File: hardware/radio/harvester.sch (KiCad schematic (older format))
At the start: 39 parts, among them Q201 BSH105, U201 LTC3331

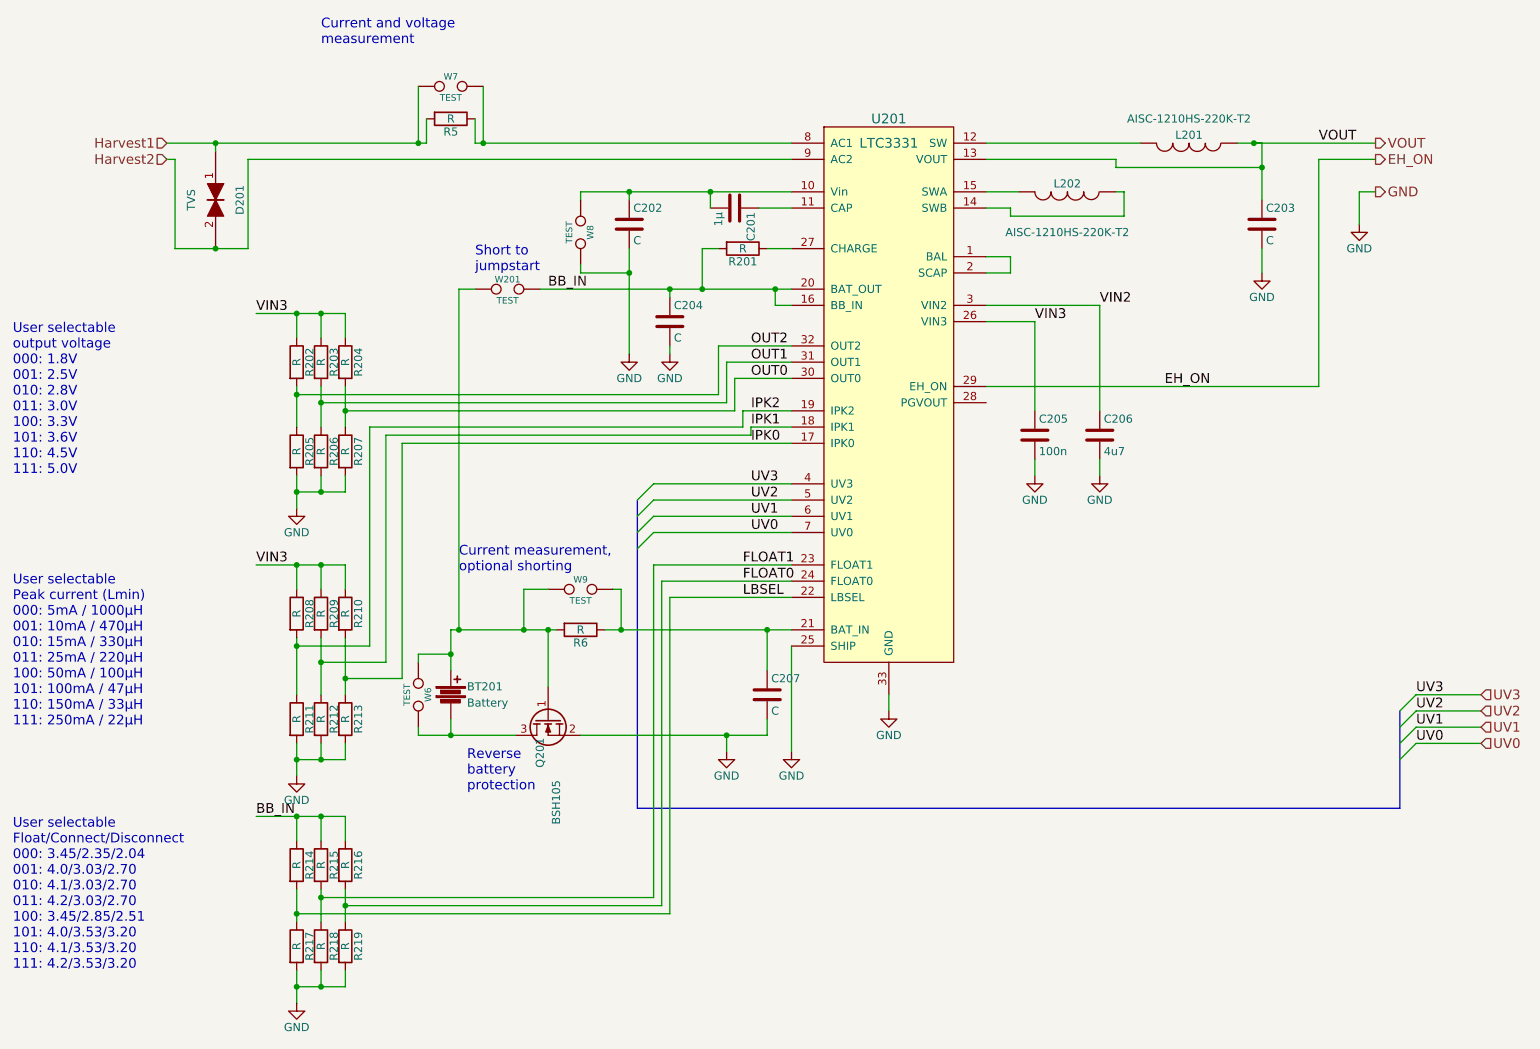
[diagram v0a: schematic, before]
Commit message: compress schematic for embedding images in thesis
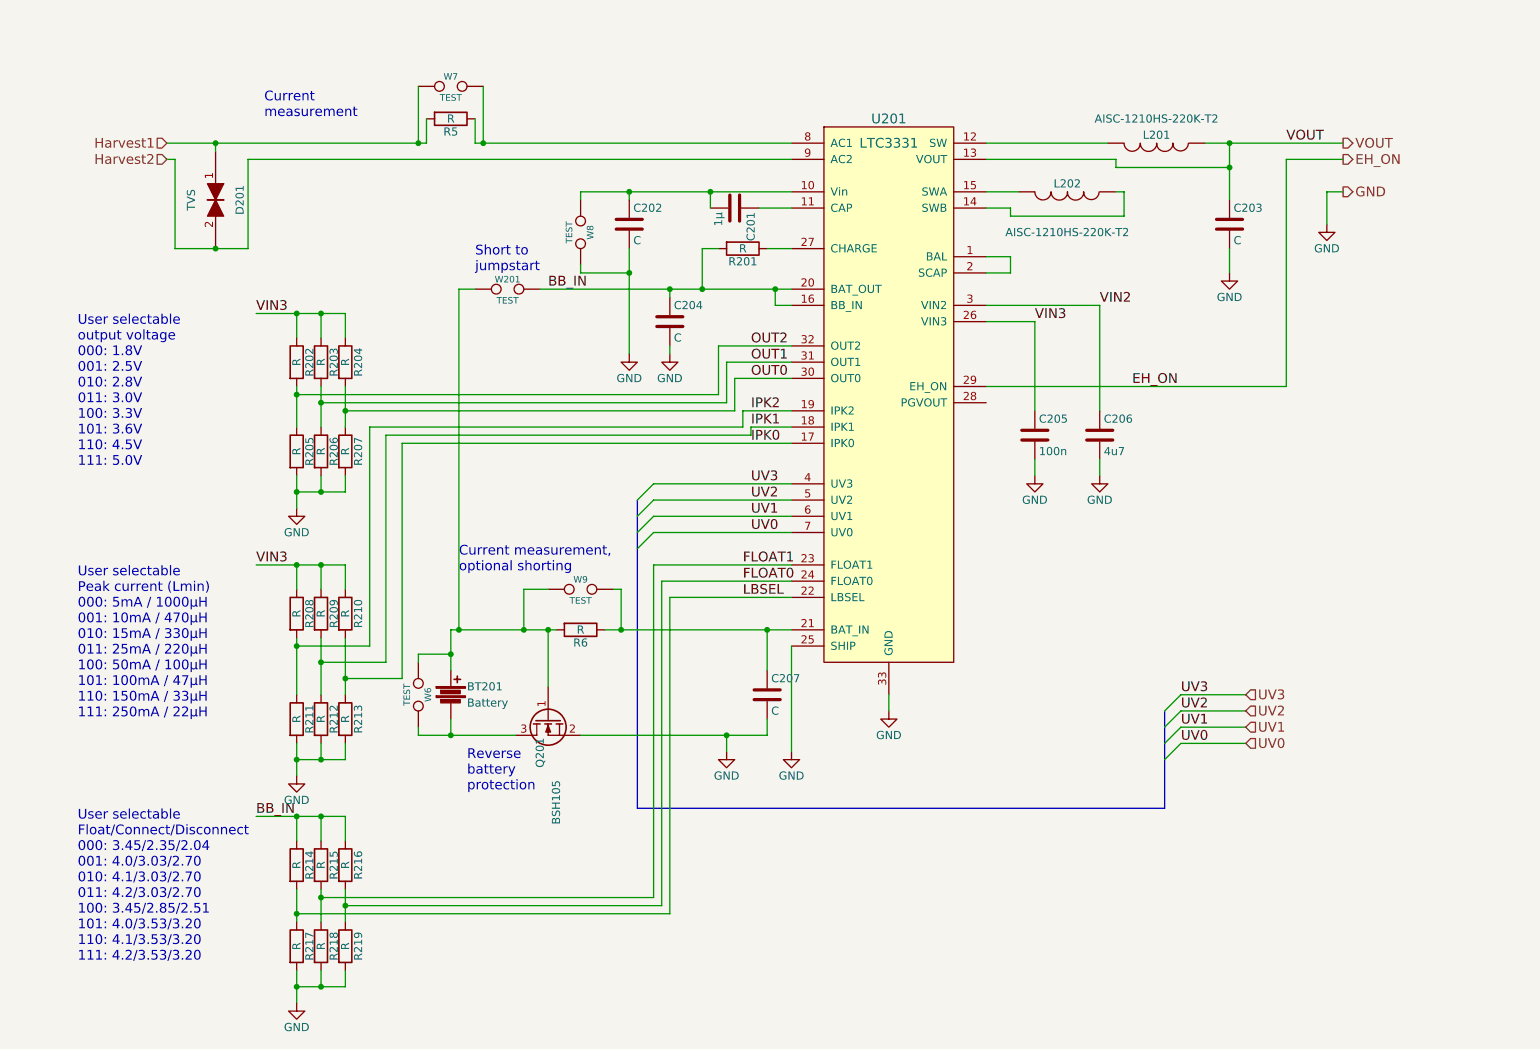
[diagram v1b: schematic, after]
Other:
- note added: "Current\nmeasurement"
- note removed: "Current and voltage \nmeasurement"
- moved on the sheet: C203, L201
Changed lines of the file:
@@
 	1    0    0    -1
 $EndComp
-Text Notes 1100 4250 0    60   ~ 0
+Text Notes 1500 4200 0    60   ~ 0
 User selectable \noutput voltage\n000: 1.8V\n001: 2.5V\n010: 2.8V\n011: 3.0V\n100: 3.3V\n101: 3.6V\n110: 4.5V\n111: 5.0V
 Text Label 2600 3250 0    60   ~ 0
@@
 	1    0    0    -1
 $EndComp
-Text Notes 1100 7300 0    60   ~ 0
+Text Notes 1500 7250 0    60   ~ 0
 User selectable \nFloat/Connect/Disconnect\n000: 3.45/2.35/2.04\n001: 4.0/3.03/2.70\n010: 4.1/3.03/2.70\n011: 4.2/3.03/2.70\n100: 3.45/2.85/2.51\n101: 4.0/3.53/3.20\n110: 4.1/3.53/3.20\n111: 4.2/3.53/3.20
 $Comp
@@
 	1    0    0    -1
 $EndComp
-Text Notes 1100 5800 0    60   ~ 0
+Text Notes 1500 5750 0    60   ~ 0
 User selectable \nPeak current (Lmin)\n000: 5mA / 1000µH\n001: 10mA / 470µH\n010: 15mA / 330µH\n011: 25mA / 220µH\n100: 50mA / 100µH\n101: 100mA / 47µH\n110: 150mA / 33µH\n111: 250mA / 22µH
 Text Label 5650 3450 0    60   ~ 0
@@
 L INDUCTOR L201
 U 1 1 55EA045E
-P 8350 2200
-F 0 "L201" V 8300 2200 50  0000 C CNN
-F 1 "AISC-1210HS-220K-T2" V 8200 2200 50  0000 C CNN
-F 2 "Resistors_SMD:R_1210" H 8350 2200 60  0001 C CNN
-F 3 "" H 8350 2200 60  0000 C CNN
-	1    8350 2200
+P 8150 2200
+F 0 "L201" V 8100 2200 50  0000 C CNN
+F 1 "AISC-1210HS-220K-T2" V 8000 2200 50  0000 C CNN
+F 2 "Resistors_SMD:R_1210" H 8150 2200 60  0001 C CNN
+F 3 "" H 8150 2200 60  0000 C CNN
+	1    8150 2200
 	0    1    1    0
 $EndComp
@@
 L C C203
 U 1 1 55EA08DD
-P 8800 2700
-F 0 "C203" H 8825 2800 50  0000 L CNN
-F 1 "C" H 8825 2600 50  0000 L CNN
-F 2 "Capacitors_SMD:C_0603" H 8838 2550 30  0001 C CNN
-F 3 "" H 8800 2700 60  0000 C CNN
-	1    8800 2700
+P 8600 2700
+F 0 "C203" H 8625 2800 50  0000 L CNN
+F 1 "C" H 8625 2600 50  0000 L CNN
+F 2 "Capacitors_SMD:C_0603" H 8638 2550 30  0001 C CNN
+F 3 "" H 8600 2700 60  0000 C CNN
+	1    8600 2700
 	1    0    0    -1
 $EndComp
@@
 L GND #PWR020
 U 1 1 55EA0A97
-P 8800 3000
-F 0 "#PWR020" H 8800 2750 50  0001 C CNN
-F 1 "GND" H 8800 2850 50  0000 C CNN
-F 2 "" H 8800 3000 60  0000 C CNN
-F 3 "" H 8800 3000 60  0000 C CNN
-	1    8800 3000
+P 8600 3000
+F 0 "#PWR020" H 8600 2750 50  0001 C CNN
+F 1 "GND" H 8600 2850 50  0000 C CNN
+F 2 "" H 8600 3000 60  0000 C CNN
+F 3 "" H 8600 3000 60  0000 C CNN
+	1    8600 3000
 	1    0    0    -1
 $EndComp
@@
 	1    0    0    -1
 $EndComp
-Text Label 8200 3700 0    60   ~ 0
+Text Label 8000 3700 0    60   ~ 0
 EH_ON
 Text Label 7800 3200 0    60   ~ 0
@@
 Text Label 7400 3300 0    60   ~ 0
 VIN3
-Text Label 9150 2200 0    60   ~ 0
+Text Label 8950 2200 0    60   ~ 0
 VOUT
 Entry Wire Line
-	9650 5700 9750 5600
+	8200 5700 8300 5600
 Entry Wire Line
-	9650 5800 9750 5700
+	8200 5800 8300 5700
 Entry Wire Line
-	9650 5900 9750 5800
+	8200 5900 8300 5800
 Entry Wire Line
-	9650 6000 9750 5900
+	8200 6000 8300 5900
 Entry Wire Line
 	4950 4700 5050 4600
@@
 Entry Wire Line
 	4950 4400 5050 4300
-Text Label 9750 5600 0    60   ~ 0
+Text Label 8300 5600 0    60   ~ 0
 UV3
-Text Label 9750 5700 0    60   ~ 0
+Text Label 8300 5700 0    60   ~ 0
 UV2
-Text Label 9750 5800 0    60   ~ 0
+Text Label 8300 5800 0    60   ~ 0
 UV1
-Text Label 9750 5900 0    60   ~ 0
+Text Label 8300 5900 0    60   ~ 0
 UV0
-Text HLabel 10150 5600 2    60   Input ~ 0
+Text HLabel 8700 5600 2    60   Input ~ 0
 UV3
-Text HLabel 10150 5700 2    60   Input ~ 0
+Text HLabel 8700 5700 2    60   Input ~ 0
 UV2
-Text HLabel 10150 5800 2    60   Input ~ 0
+Text HLabel 8700 5800 2    60   Input ~ 0
 UV1
-Text HLabel 10150 5900 2    60   Input ~ 0
+Text HLabel 8700 5900 2    60   Input ~ 0
 UV0
-Text HLabel 9500 2200 2    60   Output ~ 0
+Text HLabel 9300 2200 2    60   Output ~ 0
 VOUT
-Text HLabel 9500 2300 2    60   Output ~ 0
+Text HLabel 9300 2300 2    60   Output ~ 0
 EH_ON
 $Comp
@@
 L GND #PWR024
 U 1 1 55EB3C4E
-P 9400 2700
-F 0 "#PWR024" H 9400 2450 50  0001 C CNN
-F 1 "GND" H 9400 2550 50  0000 C CNN
-F 2 "" H 9400 2700 60  0000 C CNN
-F 3 "" H 9400 2700 60  0000 C CNN
-	1    9400 2700
-	1    0    0    -1
-$EndComp
-Text HLabel 9500 2500 2    60   Output ~ 0
+P 9200 2700
+F 0 "#PWR024" H 9200 2450 50  0001 C CNN
+F 1 "GND" H 9200 2550 50  0000 C CNN
+F 2 "" H 9200 2700 60  0000 C CNN
+F 3 "" H 9200 2700 60  0000 C CNN
+	1    9200 2700
+	1    0    0    -1
+$EndComp
+Text HLabel 9300 2500 2    60   Output ~ 0
 GND
 Text Notes 3900 6200 0    60   ~ 0
@@
 	0    1    1    0
 $EndComp
-Text Notes 3000 1600 0    60   ~ 0
-Current and voltage \nmeasurement
+Text Notes 2650 2050 0    60   ~ 0
+Current\nmeasurement
 $Comp
 L TEST W201
@@
 	4950 4400 4950 6300
 Wire Bus Line
-	4950 6300 9650 6300
+	4950 6300 8200 6300
 Wire Bus Line
-	9650 6300 9650 5700
+	8200 6300 8200 5700
 Wire Wire Line
 	6500 5600 6500 5700
@@
 	7250 2600 7100 2600
 Wire Wire Line
-	7100 2200 8050 2200
-Wire Wire Line
-	8650 2200 8800 2200
-Wire Wire Line
-	8800 2200 8800 2550
-Wire Wire Line
-	8800 2350 7900 2350
+	7100 2200 7850 2200
+Wire Wire Line
+	8450 2200 9300 2200
+Wire Wire Line
+	8600 2200 8600 2550
+Wire Wire Line
+	8600 2350 7900 2350
 Wire Wire Line
 	7900 2350 7900 2300
 Wire Wire Line
 	7900 2300 7100 2300
-Connection ~ 8800 2350
-Wire Wire Line
-	8800 2850 8800 3000
+Connection ~ 8600 2350
+Wire Wire Line
+	8600 2850 8600 3000
 Wire Wire Line
 	5900 2850 5750 2850
@@
 	7400 3300 7400 3850
 Wire Wire Line
-	7100 3700 9150 3700
+	7100 3700 8950 3700
 Wire Wire Line
 	7100 3200 7800 3200
@@
 	7800 4150 7800 4250
 Wire Wire Line
-	8750 2200 9500 2200
-Connection ~ 8750 2200
-Wire Wire Line
-	9750 5600 10150 5600
-Wire Wire Line
-	9750 5700 10150 5700
-Wire Wire Line
-	9750 5800 10150 5800
-Wire Wire Line
-	9750 5900 10150 5900
-Wire Wire Line
-	9150 3700 9150 2300
-Wire Wire Line
-	9150 2300 9500 2300
+	8300 5600 8700 5600
+Wire Wire Line
+	8300 5700 8700 5700
+Wire Wire Line
+	8300 5800 8700 5800
+Wire Wire Line
+	8300 5900 8700 5900
+Wire Wire Line
+	8950 3700 8950 2300
+Wire Wire Line
+	8950 2300 9300 2300
 Wire Wire Line
 	5150 5000 5150 6950
@@
 Connection ~ 5500 5850
 Wire Wire Line
-	9400 2700 9400 2500
-Wire Wire Line
-	9400 2500 9500 2500
+	9200 2700 9200 2500
+Wire Wire Line
+	9200 2500 9300 2500
 Wire Wire Line
 	4600 2500 5900 2500
@@
 Text Label 2600 6350 0    60   ~ 0
 BB_IN
+Connection ~ 8600 2200
 $EndSCHEMATC

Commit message: Compress schematics for screenshots
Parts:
- C201: value 1µ -> 4µ7
- C202, C203: value C -> 22µ
- C204, C207: value C -> 4µ7
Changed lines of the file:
@@
 P 5550 2600
 F 0 "C201" H 5575 2700 50  0000 L CNN
-F 1 "1µ" H 5575 2500 50  0000 L CNN
+F 1 "4µ7" H 5575 2500 50  0000 L CNN
 F 2 "Capacitors_SMD:C_0603" H 5588 2450 30  0001 C CNN
 F 3 "" H 5550 2600 60  0000 C CNN
@@
 P 4900 2700
 F 0 "C202" H 4925 2800 50  0000 L CNN
-F 1 "C" H 4925 2600 50  0000 L CNN
+F 1 "22µ" H 4925 2600 50  0000 L CNN
 F 2 "Capacitors_SMD:C_0603" H 4938 2550 30  0001 C CNN
 F 3 "" H 4900 2700 60  0000 C CNN
@@
 P 5150 3300
 F 0 "C204" H 5175 3400 50  0000 L CNN
-F 1 "C" H 5175 3200 50  0000 L CNN
+F 1 "4µ7" H 5175 3200 50  0000 L CNN
 F 2 "Capacitors_SMD:C_0603" H 5188 3150 30  0001 C CNN
 F 3 "" H 5150 3300 60  0000 C CNN
@@
 P 8600 2700
 F 0 "C203" H 8625 2800 50  0000 L CNN
-F 1 "C" H 8625 2600 50  0000 L CNN
+F 1 "22µ" H 8625 2600 50  0000 L CNN
 F 2 "Capacitors_SMD:C_0603" H 8638 2550 30  0001 C CNN
 F 3 "" H 8600 2700 60  0000 C CNN
@@
 P 5750 5600
 F 0 "C207" H 5775 5700 50  0000 L CNN
-F 1 "C" H 5775 5500 50  0000 L CNN
+F 1 "4µ7" H 5775 5500 50  0000 L CNN
 F 2 "Capacitors_SMD:C_0603" H 5788 5450 30  0001 C CNN
 F 3 "" H 5750 5600 60  0000 C CNN
